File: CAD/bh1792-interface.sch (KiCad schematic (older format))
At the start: 8 parts

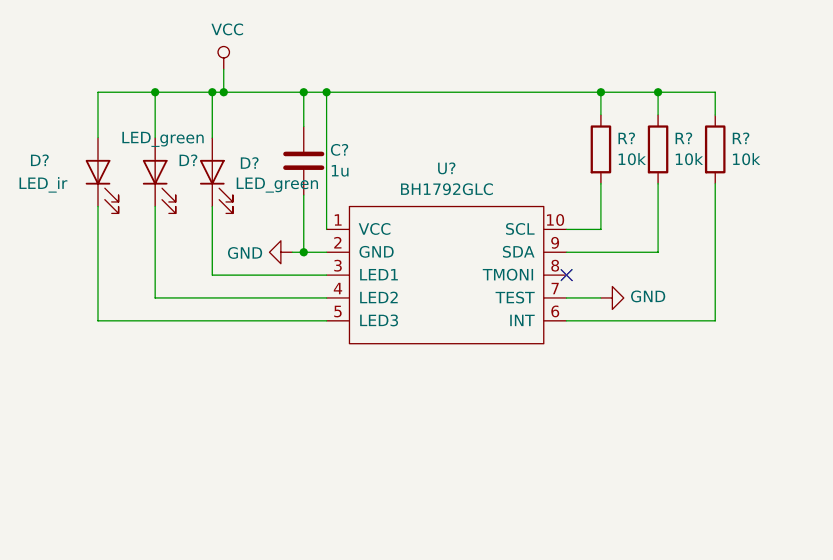
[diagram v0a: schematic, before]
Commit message: Created Power PCB, both schematic and layout
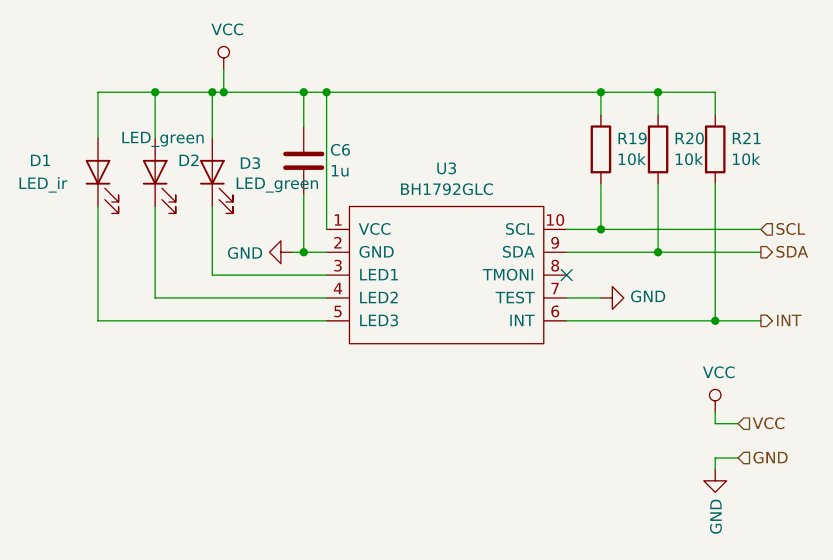
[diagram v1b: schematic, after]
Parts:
- C6: renamed from C?; footprint (none) -> Capacitor_SMD:C_0603_1608Metric
- D1, D2, D3: renamed from D?; footprint (none) -> Diode_SMD:D_0603_1608Metric
- R19, R20, R21: renamed from R?; footprint (none) -> Resistor_SMD:R_0603_1608Metric
- U3: renamed from U?; footprint (none) -> Package_DFN_QFN:DFN-10-1EP_3x3mm_P0.5mm_EP1.75x2.7mm
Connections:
- net SCL: now reaches R19.2, U3.10 (SCL)
- net INT: now reaches R21.2, U3.6 (INT)
- net SDA: now reaches R20.2, U3.9 (SDA)
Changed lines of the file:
@@
 $Descr A4 11693 8268
 encoding utf-8
-Sheet 2 2
+Sheet 2 4
 Title ""
 Date ""
@@
 U 1 1 5CD03E93
 P 6000 3700
-F 0 "U?" H 5975 4165 50  0000 C CNN
+AR Path="/5CD03E93" Ref="U?"  Part="1"
+AR Path="/5CD03BDA/5CD03E93" Ref="U3"  Part="1"
+F 0 "U3" H 5975 4165 50  0000 C CNN
 F 1 "BH1792GLC" H 5975 4074 50  0000 C CNN
-F 2 "" H 6000 3700 50  0001 C CNN
+F 2 "Package_DFN_QFN:DFN-10-1EP_3x3mm_P0.5mm_EP1.75x2.7mm" H 6000 3700 50  0001 C CNN
 F 3 "" H 6000 3700 50  0001 C CNN
 	1    6000 3700
@@
 $EndComp
 $Comp
-L Device:LED D?
+L Device:LED D1
 U 1 1 5CD03E9A
 P 4450 3250
-F 0 "D?" V 4500 3550 50  0000 R CNN
+F 0 "D1" V 4500 3550 50  0000 R CNN
 F 1 "LED_ir" V 4400 3600 50  0000 R CNN
-F 2 "" H 4450 3250 50  0001 C CNN
+F 2 "Diode_SMD:D_0603_1608Metric" H 4450 3250 50  0001 C CNN
 F 3 "~" H 4450 3250 50  0001 C CNN
 	1    4450 3250
@@
 	4450 3900 5450 3900
 $Comp
-L Device:LED D?
+L Device:LED D2
 U 1 1 5CD03EA6
 P 4700 3250
-F 0 "D?" V 4750 3150 50  0000 R CNN
+F 0 "D2" V 4750 3150 50  0000 R CNN
 F 1 "LED_green" V 4850 3400 50  0000 R CNN
-F 2 "" H 4700 3250 50  0001 C CNN
+F 2 "Diode_SMD:D_0603_1608Metric" H 4700 3250 50  0001 C CNN
 F 3 "~" H 4700 3250 50  0001 C CNN
 	1    4700 3250
@@
 $EndComp
 $Comp
-L Device:LED D?
+L Device:LED D3
 U 1 1 5CD03EAD
 P 4950 3250
-F 0 "D?" V 4988 3132 50  0000 R CNN
+F 0 "D3" V 4988 3132 50  0000 R CNN
 F 1 "LED_green" V 4900 3150 50  0000 R CNN
-F 2 "" H 4950 3250 50  0001 C CNN
+F 2 "Diode_SMD:D_0603_1608Metric" H 4950 3250 50  0001 C CNN
 F 3 "~" H 4950 3250 50  0001 C CNN
 	1    4950 3250
@@
 Connection ~ 4950 2900
 $Comp
-L power:GND #PWR?
+L power:GND #PWR0101
 U 1 1 5CD03EBD
 P 5300 3600
-F 0 "#PWR?" H 5300 3350 50  0001 C CNN
+F 0 "#PWR0101" H 5300 3350 50  0001 C CNN
 F 1 "GND" V 5305 3472 50  0000 R CNN
 F 2 "" H 5300 3600 50  0001 C CNN
@@
 	5300 3600 5350 3600
 $Comp
-L power:VCC #PWR?
+L power:VCC #PWR0102
 U 1 1 5CD03EC4
 P 5000 2800
-F 0 "#PWR?" H 5000 2650 50  0001 C CNN
+F 0 "#PWR0102" H 5000 2650 50  0001 C CNN
 F 1 "VCC" H 5017 2973 50  0000 C CNN
 F 2 "" H 5000 2800 50  0001 C CNN
@@
 	4700 2900 4950 2900
 $Comp
-L Device:C C?
+L Device:C C6
 U 1 1 5CD03ECE
 P 5350 3200
-F 0 "C?" H 5465 3246 50  0000 L CNN
+F 0 "C6" H 5465 3246 50  0000 L CNN
 F 1 "1u" H 5465 3155 50  0000 L CNN
-F 2 "" H 5388 3050 50  0001 C CNN
+F 2 "Capacitor_SMD:C_0603_1608Metric" H 5388 3050 50  0001 C CNN
 F 3 "~" H 5350 3200 50  0001 C CNN
 	1    5350 3200
@@
 	5350 3350 5350 3600
 $Comp
-L Device:R R?
+L Device:R R19
 U 1 1 5CD03EDB
 P 6650 3150
-F 0 "R?" H 6720 3196 50  0000 L CNN
+F 0 "R19" H 6720 3196 50  0000 L CNN
 F 1 "10k" H 6720 3105 50  0000 L CNN
-F 2 "" V 6580 3150 50  0001 C CNN
+F 2 "Resistor_SMD:R_0603_1608Metric" V 6580 3150 50  0001 C CNN
 F 3 "~" H 6650 3150 50  0001 C CNN
 	1    6650 3150
@@
 $EndComp
 $Comp
-L Device:R R?
+L Device:R R20
 U 1 1 5CD03EE2
 P 6900 3150
-F 0 "R?" H 6970 3196 50  0000 L CNN
+F 0 "R20" H 6970 3196 50  0000 L CNN
 F 1 "10k" H 6970 3105 50  0000 L CNN
-F 2 "" V 6830 3150 50  0001 C CNN
+F 2 "Resistor_SMD:R_0603_1608Metric" V 6830 3150 50  0001 C CNN
 F 3 "~" H 6900 3150 50  0001 C CNN
 	1    6900 3150
@@
 $EndComp
 $Comp
-L Device:R R?
+L Device:R R21
 U 1 1 5CD03EE9
 P 7150 3150
-F 0 "R?" H 7220 3196 50  0000 L CNN
+F 0 "R21" H 7220 3196 50  0000 L CNN
 F 1 "10k" H 7220 3105 50  0000 L CNN
-F 2 "" V 7080 3150 50  0001 C CNN
+F 2 "Resistor_SMD:R_0603_1608Metric" V 7080 3150 50  0001 C CNN
 F 3 "~" H 7150 3150 50  0001 C CNN
 	1    7150 3150
@@
 	7150 3900 7150 3300
 $Comp
-L power:GND #PWR?
+L power:GND #PWR0103
 U 1 1 5CD03EFF
 P 6650 3800
-F 0 "#PWR?" H 6650 3550 50  0001 C CNN
+F 0 "#PWR0103" H 6650 3550 50  0001 C CNN
 F 1 "GND" V 6655 3672 50  0000 R CNN
 F 2 "" H 6650 3800 50  0001 C CNN
@@
 	6500 3800 6650 3800
 NoConn ~ 6500 3700
+Text HLabel 7350 3500 2    50   Input ~ 0
+SCL
+Text HLabel 7350 3600 2    50   Output ~ 0
+SDA
+Text HLabel 7350 3900 2    50   Output ~ 0
+INT
+Wire Wire Line
+	7150 3900 7350 3900
+Connection ~ 7150 3900
+Wire Wire Line
+	7350 3600 6900 3600
+Connection ~ 6900 3600
+Wire Wire Line
+	6650 3500 7350 3500
+Connection ~ 6650 3500
+$Comp
+L power:VCC #PWR0104
+U 1 1 5CD0520D
+P 7150 4300
+F 0 "#PWR0104" H 7150 4150 50  0001 C CNN
+F 1 "VCC" H 7167 4473 50  0000 C CNN
+F 2 "" H 7150 4300 50  0001 C CNN
+F 3 "" H 7150 4300 50  0001 C CNN
+	1    7150 4300
+	1    0    0    -1
+$EndComp
+$Comp
+L power:GND #PWR0105
+U 1 1 5CD05228
+P 7150 4550
+F 0 "#PWR0105" H 7150 4300 50  0001 C CNN
+F 1 "GND" V 7155 4422 50  0000 R CNN
+F 2 "" H 7150 4550 50  0001 C CNN
+F 3 "" H 7150 4550 50  0001 C CNN
+	1    7150 4550
+	1    0    0    -1
+$EndComp
+Text HLabel 7250 4350 2    50   Input ~ 0
+VCC
+Text HLabel 7250 4500 2    50   Input ~ 0
+GND
+Wire Wire Line
+	7250 4350 7150 4350
+Wire Wire Line
+	7150 4350 7150 4300
+Wire Wire Line
+	7150 4550 7150 4500
+Wire Wire Line
+	7150 4500 7250 4500
 $EndSCHEMATC

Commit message: Finished PCB Draft -- waiting for review
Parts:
- C7: renamed from C6; footprint Capacitor_SMD:C_0603_1608Metric -> Capacitor_SMD:C_0402_1005Metric
- R23: renamed from R19; footprint Resistor_SMD:R_0603_1608Metric -> Resistor_SMD:R_0402_1005Metric
- R24: renamed from R20; footprint Resistor_SMD:R_0603_1608Metric -> Resistor_SMD:R_0402_1005Metric
- R25: renamed from R21; footprint Resistor_SMD:R_0603_1608Metric -> Resistor_SMD:R_0402_1005Metric
- U5: renamed from U3; footprint Package_DFN_QFN:DFN-10-1EP_3x3mm_P0.5mm_EP1.75x2.7mm -> BH1790GLC-E2:PQFN70P280X280X100-10N
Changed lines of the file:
@@
 EESchema Schematic File Version 4
 LIBS:HealthMonitor-cache
+LIBS:Max86141-cache
 EELAYER 26 0
 EELAYER END
 $Descr A4 11693 8268
 encoding utf-8
-Sheet 2 4
+Sheet 3 7
 Title ""
 Date ""
@@
 $EndDescr
 $Comp
-L HealthMonitor-rescue:BH1792GLC-bh1792glc U?
-U 1 1 5CD03E93
-P 6000 3700
-AR Path="/5CD03E93" Ref="U?"  Part="1"
-AR Path="/5CD03BDA/5CD03E93" Ref="U3"  Part="1"
-F 0 "U3" H 5975 4165 50  0000 C CNN
-F 1 "BH1792GLC" H 5975 4074 50  0000 C CNN
-F 2 "Package_DFN_QFN:DFN-10-1EP_3x3mm_P0.5mm_EP1.75x2.7mm" H 6000 3700 50  0001 C CNN
-F 3 "" H 6000 3700 50  0001 C CNN
-	1    6000 3700
-	1    0    0    -1
-$EndComp
-$Comp
 L Device:LED D1
 U 1 1 5CD03E9A
@@
 Connection ~ 4950 2900
 $Comp
-L power:GND #PWR0101
+L power:GND #PWR027
 U 1 1 5CD03EBD
 P 5300 3600
-F 0 "#PWR0101" H 5300 3350 50  0001 C CNN
+F 0 "#PWR027" H 5300 3350 50  0001 C CNN
 F 1 "GND" V 5305 3472 50  0000 R CNN
 F 2 "" H 5300 3600 50  0001 C CNN
@@
 	5300 3600 5350 3600
 $Comp
-L power:VCC #PWR0102
+L power:VCC #PWR026
 U 1 1 5CD03EC4
 P 5000 2800
-F 0 "#PWR0102" H 5000 2650 50  0001 C CNN
+F 0 "#PWR026" H 5000 2650 50  0001 C CNN
 F 1 "VCC" H 5017 2973 50  0000 C CNN
 F 2 "" H 5000 2800 50  0001 C CNN
@@
 	4700 2900 4950 2900
 $Comp
-L Device:C C6
+L Device:C C7
 U 1 1 5CD03ECE
 P 5350 3200
-F 0 "C6" H 5465 3246 50  0000 L CNN
+F 0 "C7" H 5465 3246 50  0000 L CNN
 F 1 "1u" H 5465 3155 50  0000 L CNN
-F 2 "Capacitor_SMD:C_0603_1608Metric" H 5388 3050 50  0001 C CNN
+F 2 "Capacitor_SMD:C_0402_1005Metric" H 5388 3050 50  0001 C CNN
 F 3 "~" H 5350 3200 50  0001 C CNN
 	1    5350 3200
@@
 	5350 3350 5350 3600
 $Comp
-L Device:R R19
+L Device:R R23
 U 1 1 5CD03EDB
 P 6650 3150
-F 0 "R19" H 6720 3196 50  0000 L CNN
+F 0 "R23" H 6720 3196 50  0000 L CNN
 F 1 "10k" H 6720 3105 50  0000 L CNN
-F 2 "Resistor_SMD:R_0603_1608Metric" V 6580 3150 50  0001 C CNN
+F 2 "Resistor_SMD:R_0402_1005Metric" V 6580 3150 50  0001 C CNN
 F 3 "~" H 6650 3150 50  0001 C CNN
 	1    6650 3150
@@
 $EndComp
 $Comp
-L Device:R R20
+L Device:R R24
 U 1 1 5CD03EE2
 P 6900 3150
-F 0 "R20" H 6970 3196 50  0000 L CNN
+F 0 "R24" H 6970 3196 50  0000 L CNN
 F 1 "10k" H 6970 3105 50  0000 L CNN
-F 2 "Resistor_SMD:R_0603_1608Metric" V 6830 3150 50  0001 C CNN
+F 2 "Resistor_SMD:R_0402_1005Metric" V 6830 3150 50  0001 C CNN
 F 3 "~" H 6900 3150 50  0001 C CNN
 	1    6900 3150
@@
 $EndComp
 $Comp
-L Device:R R21
+L Device:R R25
 U 1 1 5CD03EE9
 P 7150 3150
-F 0 "R21" H 7220 3196 50  0000 L CNN
+F 0 "R25" H 7220 3196 50  0000 L CNN
 F 1 "10k" H 7220 3105 50  0000 L CNN
-F 2 "Resistor_SMD:R_0603_1608Metric" V 7080 3150 50  0001 C CNN
+F 2 "Resistor_SMD:R_0402_1005Metric" V 7080 3150 50  0001 C CNN
 F 3 "~" H 7150 3150 50  0001 C CNN
 	1    7150 3150
@@
 	7150 3900 7150 3300
 $Comp
-L power:GND #PWR0103
+L power:GND #PWR028
 U 1 1 5CD03EFF
 P 6650 3800
-F 0 "#PWR0103" H 6650 3550 50  0001 C CNN
+F 0 "#PWR028" H 6650 3550 50  0001 C CNN
 F 1 "GND" V 6655 3672 50  0000 R CNN
 F 2 "" H 6650 3800 50  0001 C CNN
@@
 Connection ~ 6650 3500
 $Comp
-L power:VCC #PWR0104
+L power:VCC #PWR029
 U 1 1 5CD0520D
 P 7150 4300
-F 0 "#PWR0104" H 7150 4150 50  0001 C CNN
+F 0 "#PWR029" H 7150 4150 50  0001 C CNN
 F 1 "VCC" H 7167 4473 50  0000 C CNN
 F 2 "" H 7150 4300 50  0001 C CNN
@@
 $EndComp
 $Comp
-L power:GND #PWR0105
+L power:GND #PWR030
 U 1 1 5CD05228
 P 7150 4550
-F 0 "#PWR0105" H 7150 4300 50  0001 C CNN
+F 0 "#PWR030" H 7150 4300 50  0001 C CNN
 F 1 "GND" V 7155 4422 50  0000 R CNN
 F 2 "" H 7150 4550 50  0001 C CNN
@@
 Wire Wire Line
 	7150 4500 7250 4500
+$Comp
+L HealthMonitor-rescue:BH1792GLC-bh1792glc U?
+U 1 1 5CD03E93
+P 6000 3700
+AR Path="/5CD03E93" Ref="U?"  Part="1"
+AR Path="/5CD03BDA/5CD03E93" Ref="U?"  Part="1"
+AR Path="/5CD818DB/5CD03E93" Ref="U5"  Part="1"
+F 0 "U5" H 5975 4165 50  0000 C CNN
+F 1 "BH1792GLC" H 5975 4074 50  0000 C CNN
+F 2 "BH1790GLC-E2:PQFN70P280X280X100-10N" H 6000 3700 50  0001 C CNN
+F 3 "" H 6000 3700 50  0001 C CNN
+	1    6000 3700
+	1    0    0    -1
+$EndComp
 $EndSCHEMATC
